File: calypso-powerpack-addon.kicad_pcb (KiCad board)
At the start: 2 copper layers, 37.8 x 50.4 mm, 14 parts, among them J1 Conn_02x12_Odd_Even, J2 Conn_02x12_Odd_Even, J3 USB_B_Micro, J4 USB_A_Stacked, J5 USB_A_Stacked, J6 Conn_01x02_Pin, U1 HS8836A, U2 ESP-PSRAM32

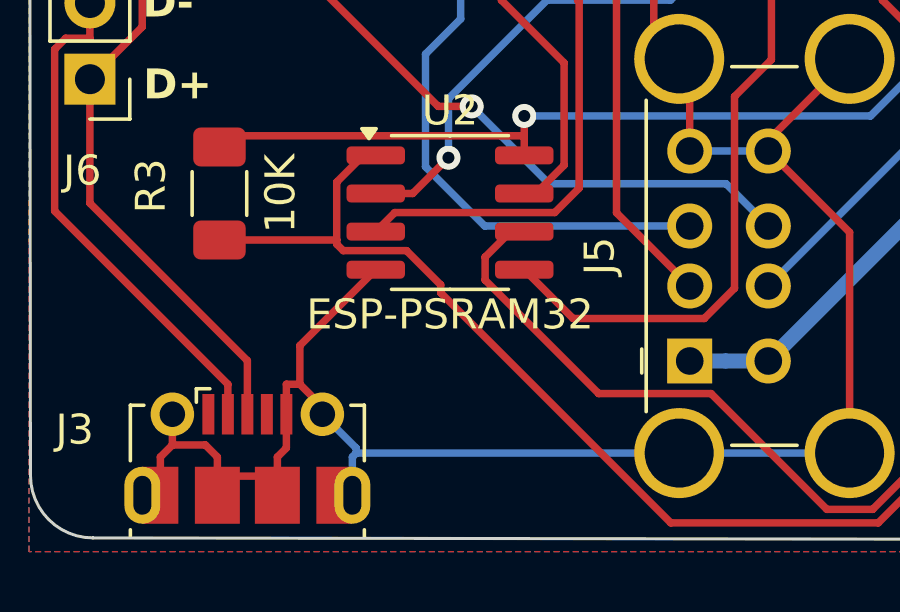
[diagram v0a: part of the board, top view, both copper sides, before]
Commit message: Fix PSRAM chip id
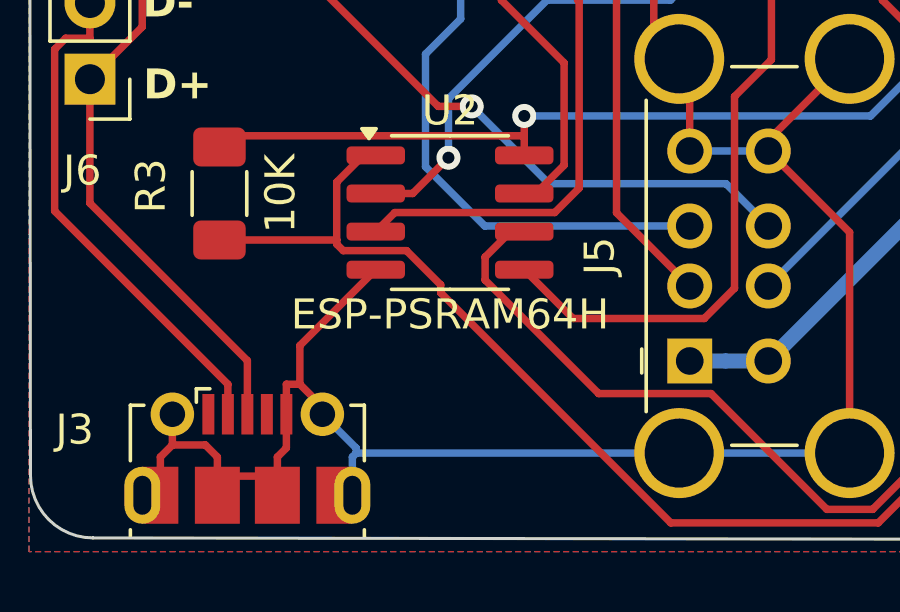
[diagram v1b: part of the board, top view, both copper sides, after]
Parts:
- U2: value ESP-PSRAM32 -> ESP-PSRAM64H
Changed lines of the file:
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@@
     (descr "Resistor SMD 1206 (3216 Metric), square (rectangular) end terminal, IPC_7351 nominal with elongated pad for handsoldering. (Body size source: IPC-SM-782 page 72, https://www.pcb-3d.com/wordpress/wp-content/uploads/ipc-sm-782a_amendment_1_and_2.pdf), generated with kicad-footprint-generator")
     (tags "resistor handsolder")
-    (property "Sheetfile" "calypso-usb-addon.kicad_sch")
+    (property "Sheetfile" "calypso-powerpack-addon.kicad_sch")
     (property "Sheetname" "")
     (property "ki_description" "Resistor")
@@
     (descr "Capacitor SMD 1206 (3216 Metric), square (rectangular) end terminal, IPC_7351 nominal with elongated pad for handsoldering. (Body size source: IPC-SM-782 page 76, https://www.pcb-3d.com/wordpress/wp-content/uploads/ipc-sm-782a_amendment_1_and_2.pdf), generated with kicad-footprint-generator")
     (tags "capacitor handsolder")
-    (property "Sheetfile" "calypso-usb-addon.kicad_sch")
+    (property "Sheetfile" "calypso-powerpack-addon.kicad_sch")
     (property "Sheetname" "")
     (property "ki_description" "Unpolarized capacitor")
@@
     (descr "Capacitor SMD 1206 (3216 Metric), square (rectangular) end terminal, IPC_7351 nominal with elongated pad for handsoldering. (Body size source: IPC-SM-782 page 76, https://www.pcb-3d.com/wordpress/wp-content/uploads/ipc-sm-782a_amendment_1_and_2.pdf), generated with kicad-footprint-generator")
     (tags "capacitor handsolder")
-    (property "Sheetfile" "calypso-usb-addon.kicad_sch")
+    (property "Sheetfile" "calypso-powerpack-addon.kicad_sch")
     (property "Sheetname" "")
     (property "ki_description" "Unpolarized capacitor")
@@
     (descr "http://www.molex.com/pdm_docs/sd/1050170001_sd.pdf")
     (tags "Micro-USB SMD Typ-B")
-    (property "Sheetfile" "calypso-usb-addon.kicad_sch")
+    (property "Sheetfile" "calypso-powerpack-addon.kicad_sch")
     (property "Sheetname" "")
     (property "ki_description" "USB Micro Type B connector")
@@
     (descr "Resistor SMD 1206 (3216 Metric), square (rectangular) end terminal, IPC_7351 nominal with elongated pad for handsoldering. (Body size source: IPC-SM-782 page 72, https://www.pcb-3d.com/wordpress/wp-content/uploads/ipc-sm-782a_amendment_1_and_2.pdf), generated with kicad-footprint-generator")
     (tags "resistor handsolder")
-    (property "Sheetfile" "calypso-usb-addon.kicad_sch")
+    (property "Sheetfile" "calypso-powerpack-addon.kicad_sch")
     (property "Sheetname" "")
     (property "ki_description" "Resistor")
@@
     (descr "Stacked USB A connector http://katalog.we-online.de/em/datasheet/61400826021.pdf")
     (tags "Wuerth stacked USB_A")
-    (property "Sheetfile" "calypso-usb-addon.kicad_sch")
+    (property "Sheetfile" "calypso-powerpack-addon.kicad_sch")
     (property "Sheetname" "")
     (property "ki_description" "USB Type A connector, stacked")
@@
     (descr "Capacitor SMD 1206 (3216 Metric), square (rectangular) end terminal, IPC_7351 nominal with elongated pad for handsoldering. (Body size source: IPC-SM-782 page 76, https://www.pcb-3d.com/wordpress/wp-content/uploads/ipc-sm-782a_amendment_1_and_2.pdf), generated with kicad-footprint-generator")
     (tags "capacitor handsolder")
-    (property "Sheetfile" "calypso-usb-addon.kicad_sch")
+    (property "Sheetfile" "calypso-powerpack-addon.kicad_sch")
     (property "Sheetname" "")
     (property "ki_description" "Unpolarized capacitor")
@@
     (descr "Resistor SMD 1206 (3216 Metric), square (rectangular) end terminal, IPC_7351 nominal with elongated pad for handsoldering. (Body size source: IPC-SM-782 page 72, https://www.pcb-3d.com/wordpress/wp-content/uploads/ipc-sm-782a_amendment_1_and_2.pdf), generated with kicad-footprint-generator")
     (tags "resistor handsolder")
-    (property "Sheetfile" "calypso-usb-addon.kicad_sch")
+    (property "Sheetfile" "calypso-powerpack-addon.kicad_sch")
     (property "Sheetname" "")
     (property "ki_description" "Resistor")
@@
     (descr "SOIC, 8 Pin (JEDEC MS-012AA, https://www.analog.com/media/en/package-pcb-resources/package/pkg_pdf/soic_narrow-r/r_8.pdf), generated with kicad-footprint-generator ipc_gullwing_generator.py")
     (tags "SOIC SO")
-    (property "Sheetfile" "calypso-usb-addon.kicad_sch")
+    (property "Sheetfile" "calypso-powerpack-addon.kicad_sch")
     (property "Sheetname" "")
     (property "ki_description" "32 Mbit serial pseudo SRAM device organized as 4Mx8 bits, 1.8 VCC, SOIC8 (SOP8)")
@@
         (effects (font (size 1 1) (thickness 0.15)))
     )
-    (fp_text value "ESP-PSRAM32" (at 0 3.4) (layer "F.SilkS")
+    (fp_text value "ESP-PSRAM64H" (at 0 3.4) (layer "F.SilkS")
         (effects (font (size 1 1) (thickness 0.15)))
     )
@@
     (descr "Through hole straight pin header, 1x02, 2.54mm pitch, single row")
     (tags "Through hole pin header THT 1x02 2.54mm single row")
-    (property "Sheetfile" "calypso-usb-addon.kicad_sch")
+    (property "Sheetfile" "calypso-powerpack-addon.kicad_sch")
     (property "Sheetname" "")
     (property "ki_description" "Generic connector, single row, 01x02, script generated")
@@
     (descr "Through hole straight socket strip, 2x12, 2.54mm pitch, double cols (from Kicad 4.0.7), script generated")
     (tags "Through hole socket strip THT 2x12 2.54mm double row")
-    (property "Sheetfile" "calypso-usb-addon.kicad_sch")
+    (property "Sheetfile" "calypso-powerpack-addon.kicad_sch")
     (property "Sheetname" "")
     (property "ki_description" "Generic connector, double row, 02x12, odd/even pin numbering scheme (row 1 odd numbers, row 2 even numbers), script generated (kicad-library-utils/schlib/autogen/connector/)")
@@
     (descr "Stacked USB A connector http://katalog.we-online.de/em/datasheet/61400826021.pdf")
     (tags "Wuerth stacked USB_A")
-    (property "Sheetfile" "calypso-usb-addon.kicad_sch")
+    (property "Sheetfile" "calypso-powerpack-addon.kicad_sch")
     (property "Sheetname" "")
     (property "ki_description" "USB Type A connector, stacked")
@@
     (descr "SOP, 16 Pin (https://www.diodes.com/assets/Datasheets/PAM8403.pdf), generated with kicad-footprint-generator ipc_gullwing_generator.py")
     (tags "SOP SO")
-    (property "Sheetfile" "calypso-usb-addon.kicad_sch")
+    (property "Sheetfile" "calypso-powerpack-addon.kicad_sch")
     (property "Sheetname" "")
     (property "ki_description" "USB 2.0 HUB")
@@
     (descr "Through hole straight pin header, 2x12, 2.54mm pitch, double rows")
     (tags "Through hole pin header THT 2x12 2.54mm double row")
-    (property "Sheetfile" "calypso-usb-addon.kicad_sch")
+    (property "Sheetfile" "calypso-powerpack-addon.kicad_sch")
     (property "Sheetname" "")
     (property "ki_description" "Generic connector, double row, 02x12, odd/even pin numbering scheme (row 1 odd numbers, row 2 even numbers), script generated (kicad-library-utils/schlib/autogen/connector/)")
